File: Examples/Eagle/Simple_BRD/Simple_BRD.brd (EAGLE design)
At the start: 33.7 x 26.7 mm, 3 parts

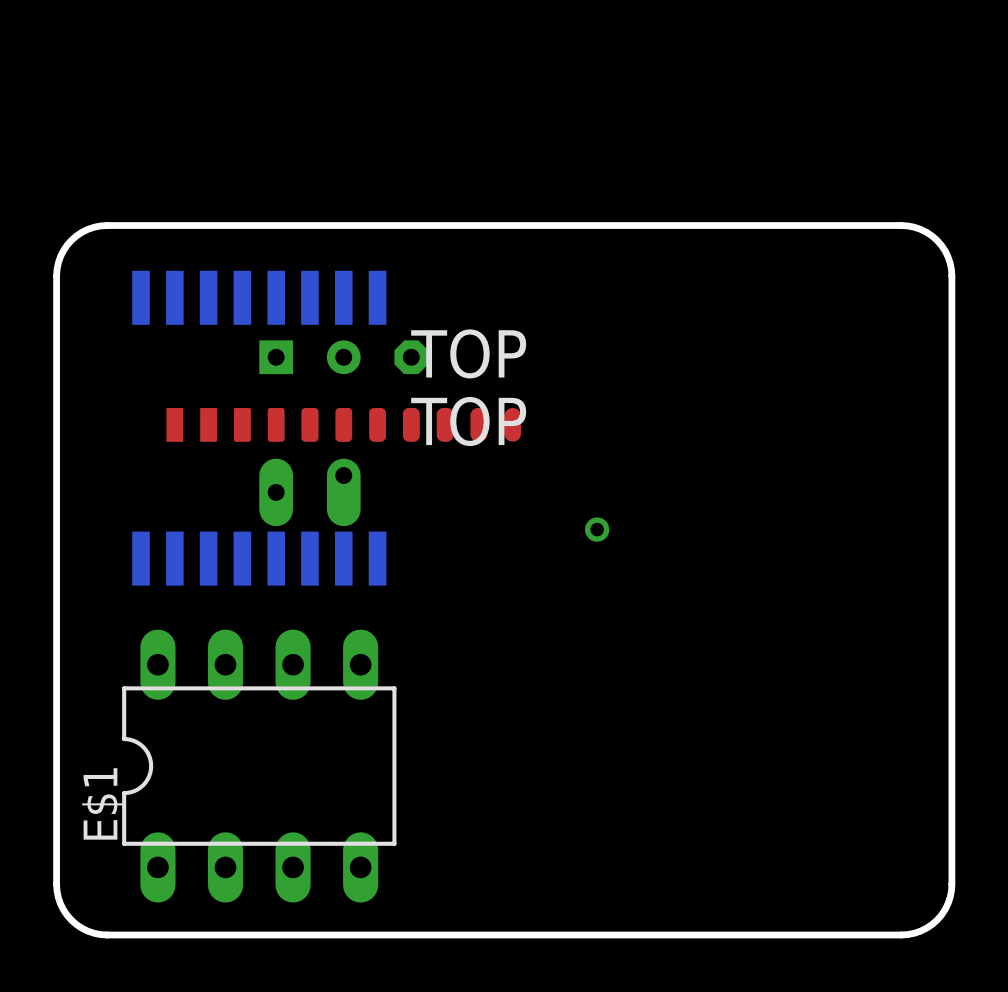
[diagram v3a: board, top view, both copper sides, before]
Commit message: Correctly rotate oblong pads
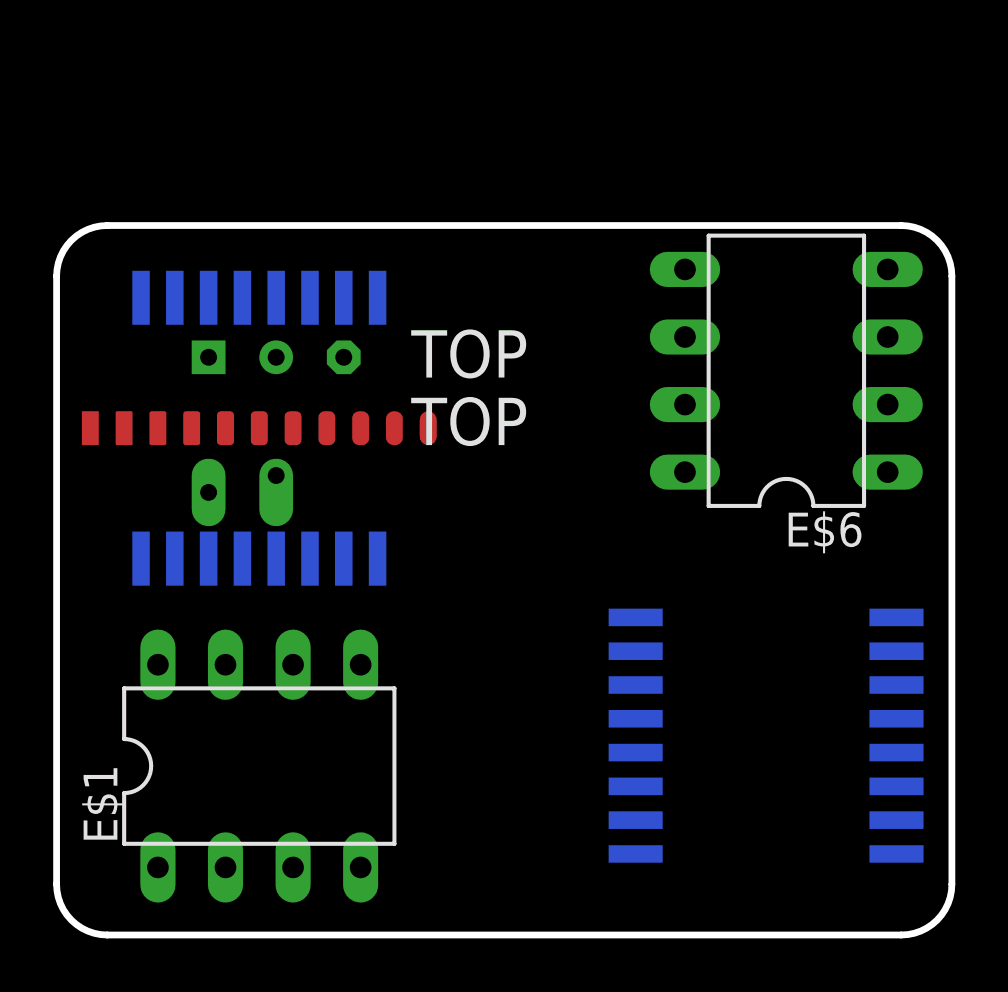
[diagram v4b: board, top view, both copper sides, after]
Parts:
- added E$4: (no value), untitled:TEST2
- added E$5: (no value), 74xx-us:SO16L
- added E$6: (no value), 74xx-us:DIL08
- moved E$3 2.54 mm to (5.71, 21.7)
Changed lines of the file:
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@@
 <setting verticaltext="up"/>
 </settings>
-<grid distance="0.05" unitdist="inch" unit="mil" style="lines" multiple="1" display="yes" altdistance="25" altunitdist="mil" altunit="mil"/>
+<grid distance="5" unitdist="mil" unit="mil" style="lines" multiple="1" display="yes" altdistance="5" altunitdist="mil" altunit="mil"/>
 <layers>
 <layer number="1" name="Top" color="4" fill="1" visible="yes" active="yes"/>
@@
 <layer number="18" name="Vias" color="2" fill="1" visible="yes" active="yes"/>
 <layer number="19" name="Unrouted" color="6" fill="1" visible="yes" active="yes"/>
-<layer number="20" name="Dimension" color="24" fill="1" visible="yes" active="yes"/>
-<layer number="21" name="tPlace" color="7" fill="1" visible="yes" active="yes"/>
-<layer number="22" name="bPlace" color="7" fill="1" visible="yes" active="yes"/>
+<layer number="20" name="Dimension" color="24" fill="1" visible="no" active="yes"/>
+<layer number="21" name="tPlace" color="7" fill="1" visible="no" active="yes"/>
+<layer number="22" name="bPlace" color="7" fill="1" visible="no" active="yes"/>
 <layer number="23" name="tOrigins" color="15" fill="1" visible="yes" active="yes"/>
 <layer number="24" name="bOrigins" color="15" fill="1" visible="yes" active="yes"/>
-<layer number="25" name="tNames" color="7" fill="1" visible="yes" active="yes"/>
-<layer number="26" name="bNames" color="7" fill="1" visible="yes" active="yes"/>
-<layer number="27" name="tValues" color="7" fill="1" visible="yes" active="yes"/>
-<layer number="28" name="bValues" color="7" fill="1" visible="yes" active="yes"/>
+<layer number="25" name="tNames" color="7" fill="1" visible="no" active="yes"/>
+<layer number="26" name="bNames" color="7" fill="1" visible="no" active="yes"/>
+<layer number="27" name="tValues" color="7" fill="1" visible="no" active="yes"/>
+<layer number="28" name="bValues" color="7" fill="1" visible="no" active="yes"/>
 <layer number="29" name="tStop" color="7" fill="3" visible="no" active="yes"/>
 <layer number="30" name="bStop" color="7" fill="6" visible="no" active="yes"/>
@@
 <layer number="37" name="tTest" color="7" fill="1" visible="no" active="yes"/>
 <layer number="38" name="bTest" color="7" fill="1" visible="no" active="yes"/>
-<layer number="39" name="tKeepout" color="4" fill="11" visible="yes" active="yes"/>
-<layer number="40" name="bKeepout" color="1" fill="11" visible="yes" active="yes"/>
-<layer number="41" name="tRestrict" color="4" fill="10" visible="yes" active="yes"/>
-<layer number="42" name="bRestrict" color="1" fill="10" visible="yes" active="yes"/>
-<layer number="43" name="vRestrict" color="2" fill="10" visible="yes" active="yes"/>
+<layer number="39" name="tKeepout" color="4" fill="11" visible="no" active="yes"/>
+<layer number="40" name="bKeepout" color="1" fill="11" visible="no" active="yes"/>
+<layer number="41" name="tRestrict" color="4" fill="10" visible="no" active="yes"/>
+<layer number="42" name="bRestrict" color="1" fill="10" visible="no" active="yes"/>
+<layer number="43" name="vRestrict" color="2" fill="10" visible="no" active="yes"/>
 <layer number="44" name="Drills" color="7" fill="1" visible="no" active="yes"/>
 <layer number="45" name="Holes" color="7" fill="1" visible="no" active="yes"/>
 <layer number="46" name="Milling" color="3" fill="1" visible="no" active="yes"/>
 <layer number="47" name="Measures" color="7" fill="1" visible="no" active="yes"/>
-<layer number="48" name="Document" color="7" fill="1" visible="yes" active="yes"/>
-<layer number="49" name="Reference" color="7" fill="1" visible="yes" active="yes"/>
-<layer number="51" name="tDocu" color="7" fill="1" visible="yes" active="yes"/>
-<layer number="52" name="bDocu" color="7" fill="1" visible="yes" active="yes"/>
+<layer number="48" name="Document" color="7" fill="1" visible="no" active="yes"/>
+<layer number="49" name="Reference" color="7" fill="1" visible="no" active="yes"/>
+<layer number="51" name="tDocu" color="7" fill="1" visible="no" active="yes"/>
+<layer number="52" name="bDocu" color="7" fill="1" visible="no" active="yes"/>
 <layer number="88" name="SimResults" color="9" fill="1" visible="no" active="no"/>
 <layer number="89" name="SimProbes" color="9" fill="1" visible="no" active="no"/>
@@
 <attribute name="VALUE" x="4.064" y="19.812" size="1.27" layer="28" ratio="10" rot="MR180"/>
 </element>
-<element name="E$3" library="untitled" package="TEST" value="" x="8.255" y="21.717" smashed="yes"/>
+<element name="E$3" library="untitled" package="TEST" value="" x="5.715" y="21.717" smashed="yes"/>
+<element name="E$4" library="untitled" package="TEST2" value="" x="7.62" y="19.05" smashed="yes"/>
+<element name="E$5" library="74xx-us" library_urn="urn:adsk.eagle:library:88" package="SO16L" package3d_urn="urn:adsk.eagle:package:17518/1" value="" x="26.67" y="7.493" smashed="yes" rot="MR90">
+<attribute name="NAME" x="23.114" y="1.905" size="1.27" layer="26" ratio="10" rot="MR180"/>
+<attribute name="VALUE" x="25.908" y="3.937" size="1.27" layer="28" ratio="10" rot="MR90"/>
+</element>
+<element name="E$6" library="74xx-us" library_urn="urn:adsk.eagle:library:88" package="DIL08" package3d_urn="urn:adsk.eagle:package:29519/2" value="" x="27.432" y="21.209" smashed="yes" rot="R90">
+<attribute name="NAME" x="30.353" y="15.875" size="1.27" layer="25" ratio="10" rot="R180"/>
+<attribute name="VALUE" x="28.067" y="17.653" size="1.27" layer="27" ratio="10" rot="R90"/>
+</element>
 </elements>
 <signals>
-<signal name="S$1">
-<via x="20.32" y="15.24" extent="1-16" drill="0.508"/>
-</signal>
 </signals>
 <mfgpreviewcolors>
